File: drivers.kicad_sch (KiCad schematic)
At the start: 14 parts, among them J10 MOLEX10POS, J11 MOLEX10POS, J4 MOLEX10POS, J5 MOLEX10POS, J6 MOLEX10POS, J7 MOLEX10POS, J8 MOLEX10POS, J9 MOLEX10POS, U4 74LVC8T245PW-Q100J, U5 74LVC8T245PW-Q100J, U6 74LVC8T245PW-Q100J

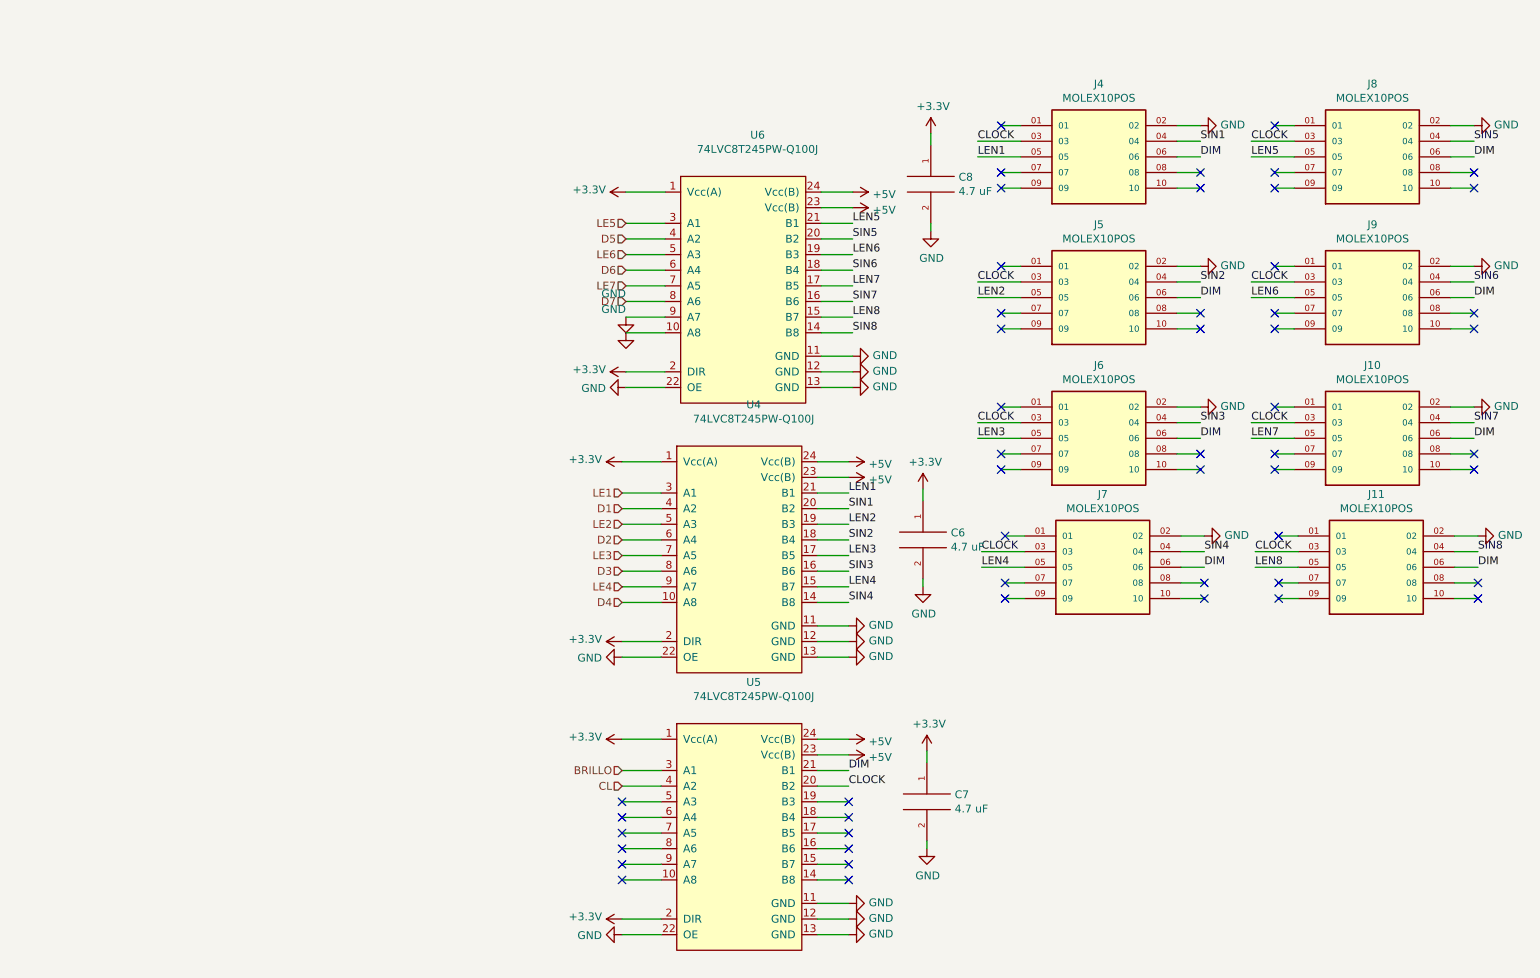
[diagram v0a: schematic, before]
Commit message: WIP: J18/Q2/Q3/R30/R31 + reguardado KiCad de todas las hojas
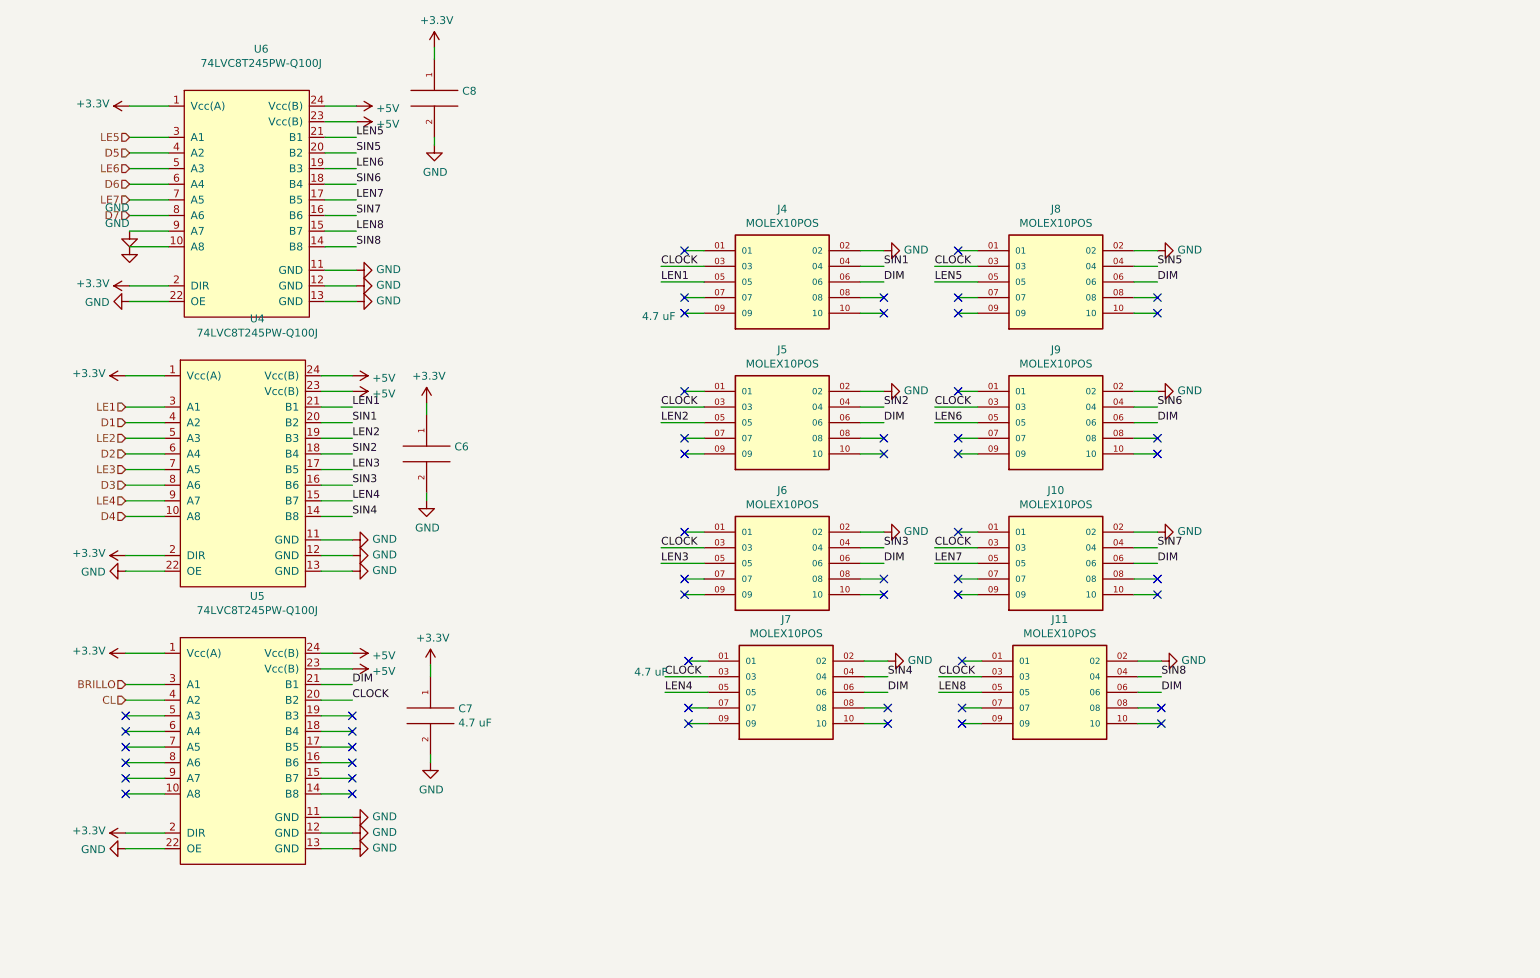
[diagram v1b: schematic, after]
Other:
- moved on the sheet: C6, C7, C8, J10, J11, J4, J5, J6, J7, J8, J9, U4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

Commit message: friday changes
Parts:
- C6, C7, C8: DigiKey (none) -> 490-14466-2-ND; MPN (none) -> GRM21BR71C475KE51L; Manufacturer (none) -> Murata Electronics
- J10, J11, J4, J5, J6, J7, J8, J9: DigiKey (none) -> 2223-SSK01-MPH-254-A10-ND; MPN (none) -> SSK01-MPH-254-A10; Manufacturer (none) -> Same Sky (Formerly CUI Devices)
- U4, U5, U6: DigiKey (none) -> 1727-8095-2-ND

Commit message: schematic updated
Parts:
- renumbered C6 to C33, C7 to C34, C8 to C35, J9 to J10, J10 to J11, J11 to J12, J4 to J5, J5 to J6, J6 to J7, J7 to J8, J8 to J9, U4 to U5, U5 to U6, U6 to U7

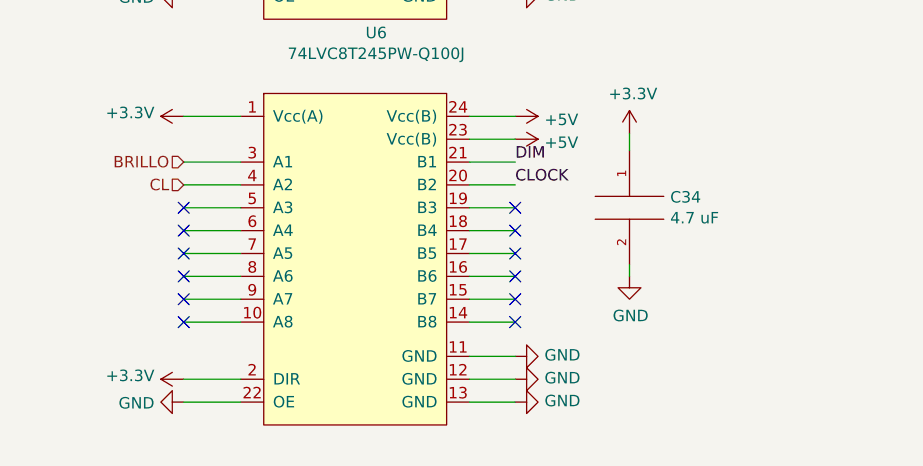
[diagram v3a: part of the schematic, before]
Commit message: 2 power source
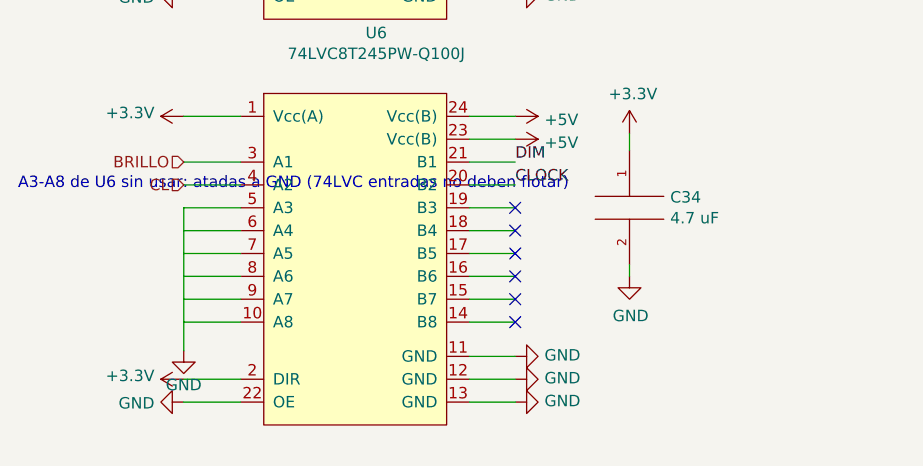
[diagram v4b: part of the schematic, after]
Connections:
- net GND: now also U6.10 (A8), U6.5 (A3), U6.6 (A4), U6.7 (A5), U6.8 (A6), U6.9 (A7)
- no-connect marks 52 -> 46
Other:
- note added: "A3-A8 de U6 sin usar: atadas a GND (74LVC entradas no deben flotar)"
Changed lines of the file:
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@@
 		(comment 4 "c")
 	)
+	(text "A3-A8 de U6 sin usar: atadas a GND (74LVC entradas no deben flotar)"
+		(exclude_from_sim no)
+		(at 45.72 134.62 0)
+		(effects
+			(font
+				(size 1.27 1.27)
+			)
+			(justify left bottom)
+		)
+	)
 	(no_connect
 		(at 154.94 68.58)
@@
 	)
 	(no_connect
-		(at 64.135 141.605)
-	)
-	(no_connect
 		(at 231.775 68.58)
 	)
@@
 	)
 	(no_connect
-		(at 64.135 149.225)
-	)
-	(no_connect
 		(at 154.94 60.96)
 	)
@@
 	)
 	(no_connect
-		(at 64.135 146.685)
-	)
-	(no_connect
 		(at 100.965 144.145)
 	)
@@
 	)
 	(no_connect
-		(at 64.135 144.145)
-	)
-	(no_connect
 		(at 155.575 137.795)
 	)
@@
 	)
 	(no_connect
-		(at 64.135 136.525)
-	)
-	(no_connect
 		(at 154.94 93.98)
 	)
@@
 	)
 	(no_connect
-		(at 64.135 139.065)
-	)
-	(no_connect
 		(at 100.965 136.525)
 	)
@@
 	(wire
 		(pts
+			(xy 64.135 136.525) (xy 64.135 139.065)
+		)
+		(stroke
+			(width 0)
+			(type default)
+		)
+	)
+	(wire
+		(pts
+			(xy 64.135 139.065) (xy 64.135 141.605)
+		)
+		(stroke
+			(width 0)
+			(type default)
+		)
+	)
+	(wire
+		(pts
+			(xy 64.135 141.605) (xy 64.135 144.145)
+		)
+		(stroke
+			(width 0)
+			(type default)
+		)
+	)
+	(wire
+		(pts
+			(xy 64.135 144.145) (xy 64.135 146.685)
+		)
+		(stroke
+			(width 0)
+			(type default)
+		)
+	)
+	(wire
+		(pts
+			(xy 64.135 146.685) (xy 64.135 149.225)
+		)
+		(stroke
+			(width 0)
+			(type default)
+		)
+	)
+	(wire
+		(pts
+			(xy 64.135 149.225) (xy 64.135 152.4)
+		)
+		(stroke
+			(width 0)
+			(type default)
+		)
+	)
+	(wire
+		(pts
 			(xy 183.515 68.58) (xy 187.325 68.58)
 		)
@@
 					(unit 1)
 				)
+			)
+		)
+	)
+	(symbol
+		(lib_id "power:GND")
+		(at 64.135 152.4 0)
+		(unit 1)
+		(exclude_from_sim no)
+		(in_bom yes)
+		(on_board yes)
+		(dnp no)
+		(property "Reference" "#PWR0180"
+			(at 64.135 158.75 0)
+			(effects
+				(font
+					(size 1.27 1.27)
+				)
+				(hide yes)
+			)
+		)
+		(property "Value" "GND"
+			(at 64.135 156.21 0)
+			(effects
+				(font
+					(size 1.27 1.27)
+				)
+			)
+		)
+		(property "Footprint" ""
+			(at 64.135 152.4 0)
+			(effects
+				(font
+					(size 1.27 1.27)
+				)
+				(hide yes)
+			)
+		)
+		(property "Datasheet" ""
+			(at 64.135 152.4 0)
+			(effects
+				(font
+					(size 1.27 1.27)
+				)
+				(hide yes)
+			)
+		)
+		(property "Description" ""
+			(at 64.135 152.4 0)
+			(effects
+				(font
+					(size 1.27 1.27)
+				)
+				(hide yes)
+			)
+		)
+		(pin "1"
+		)
+		(instances
+			(project "controlcarreta"
+				(path "/9232987b-e923-413e-abd9-77ced6cc4c47/8f78b2b0-68fd-499f-8fad-119f05b8293f"
+					(reference "#PWR0180")
+					(unit 1)
+				)
